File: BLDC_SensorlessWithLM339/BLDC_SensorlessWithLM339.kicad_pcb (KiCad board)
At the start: 2 copper layers, 48 parts, among them J1 Conn_01x04_Female, J2 Conn_01x07_Female, J3 Screw_Terminal_01x02, J4 Screw_Terminal_01x03, Q1 50N06, Q2 50N06, Q3 50N06, Q4 50N06, Q5 50N06, Q6 50N06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

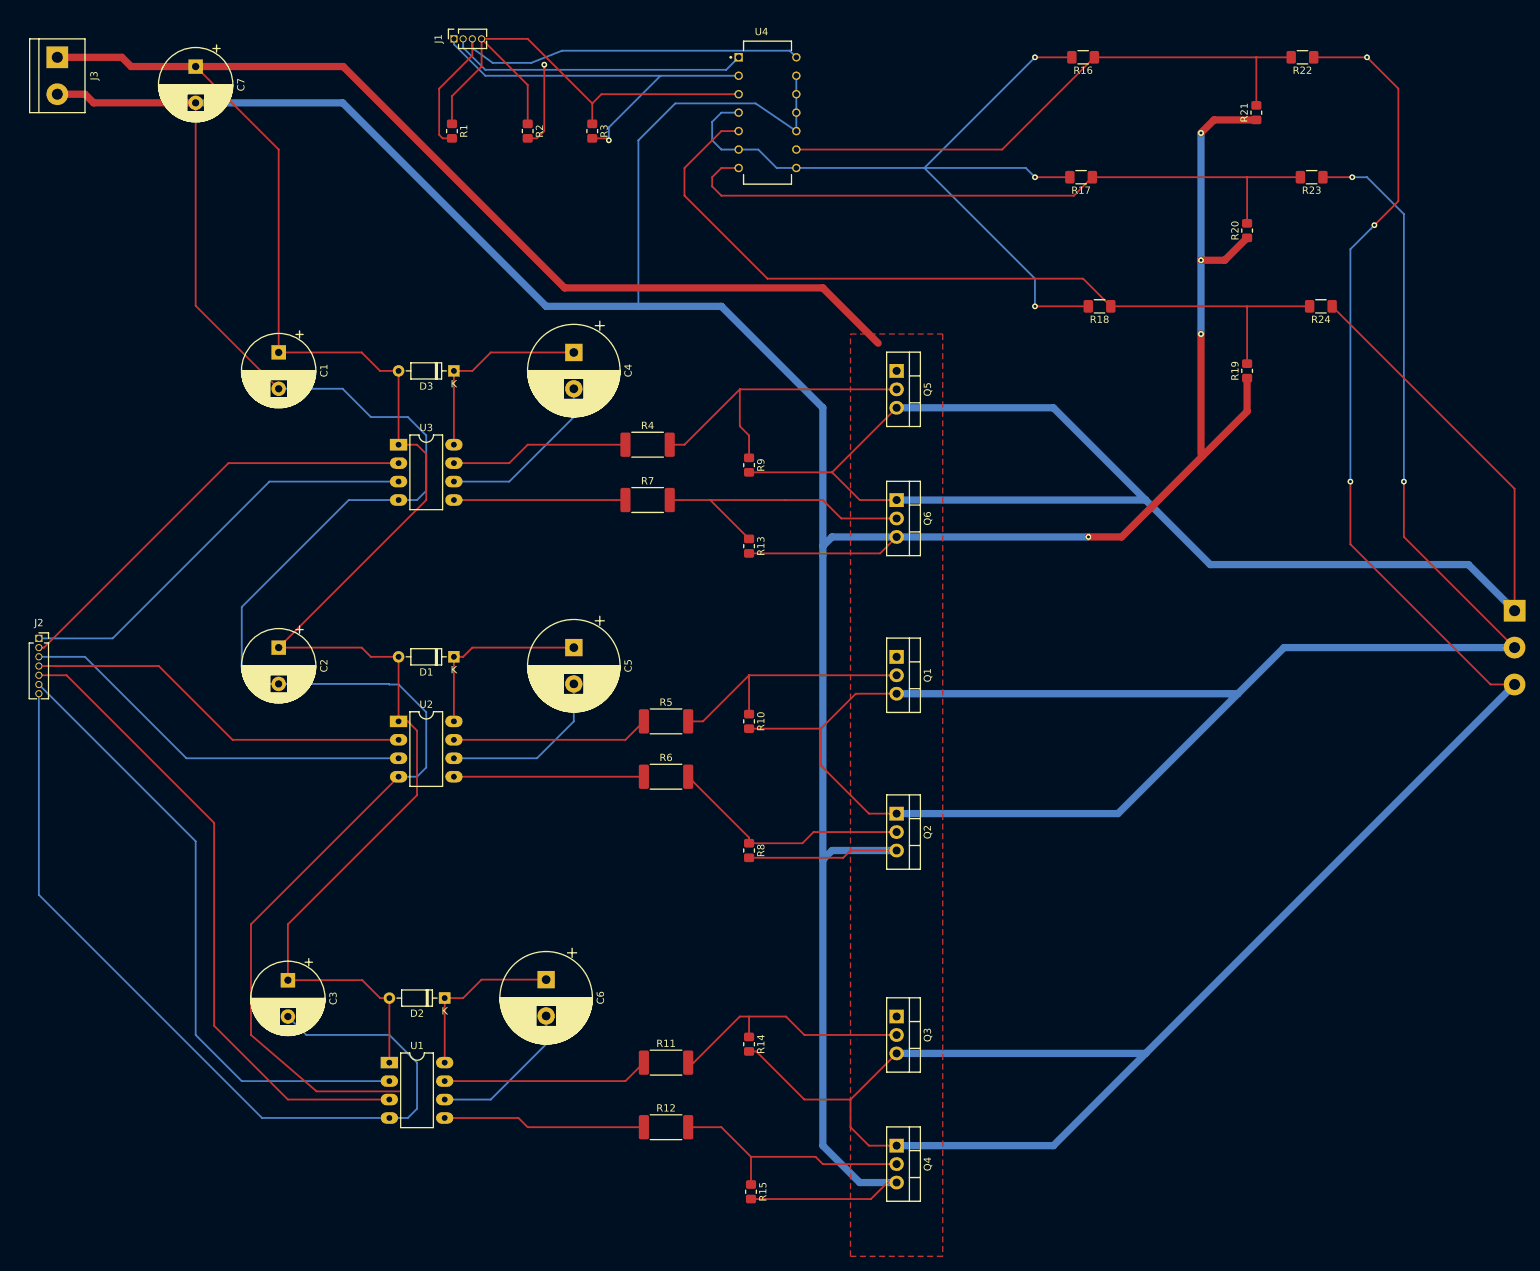
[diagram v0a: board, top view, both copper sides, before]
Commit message: Updated to Version 0.2
Updated to version 0.2. Now pcb holds only 10x10 cm^2 field.
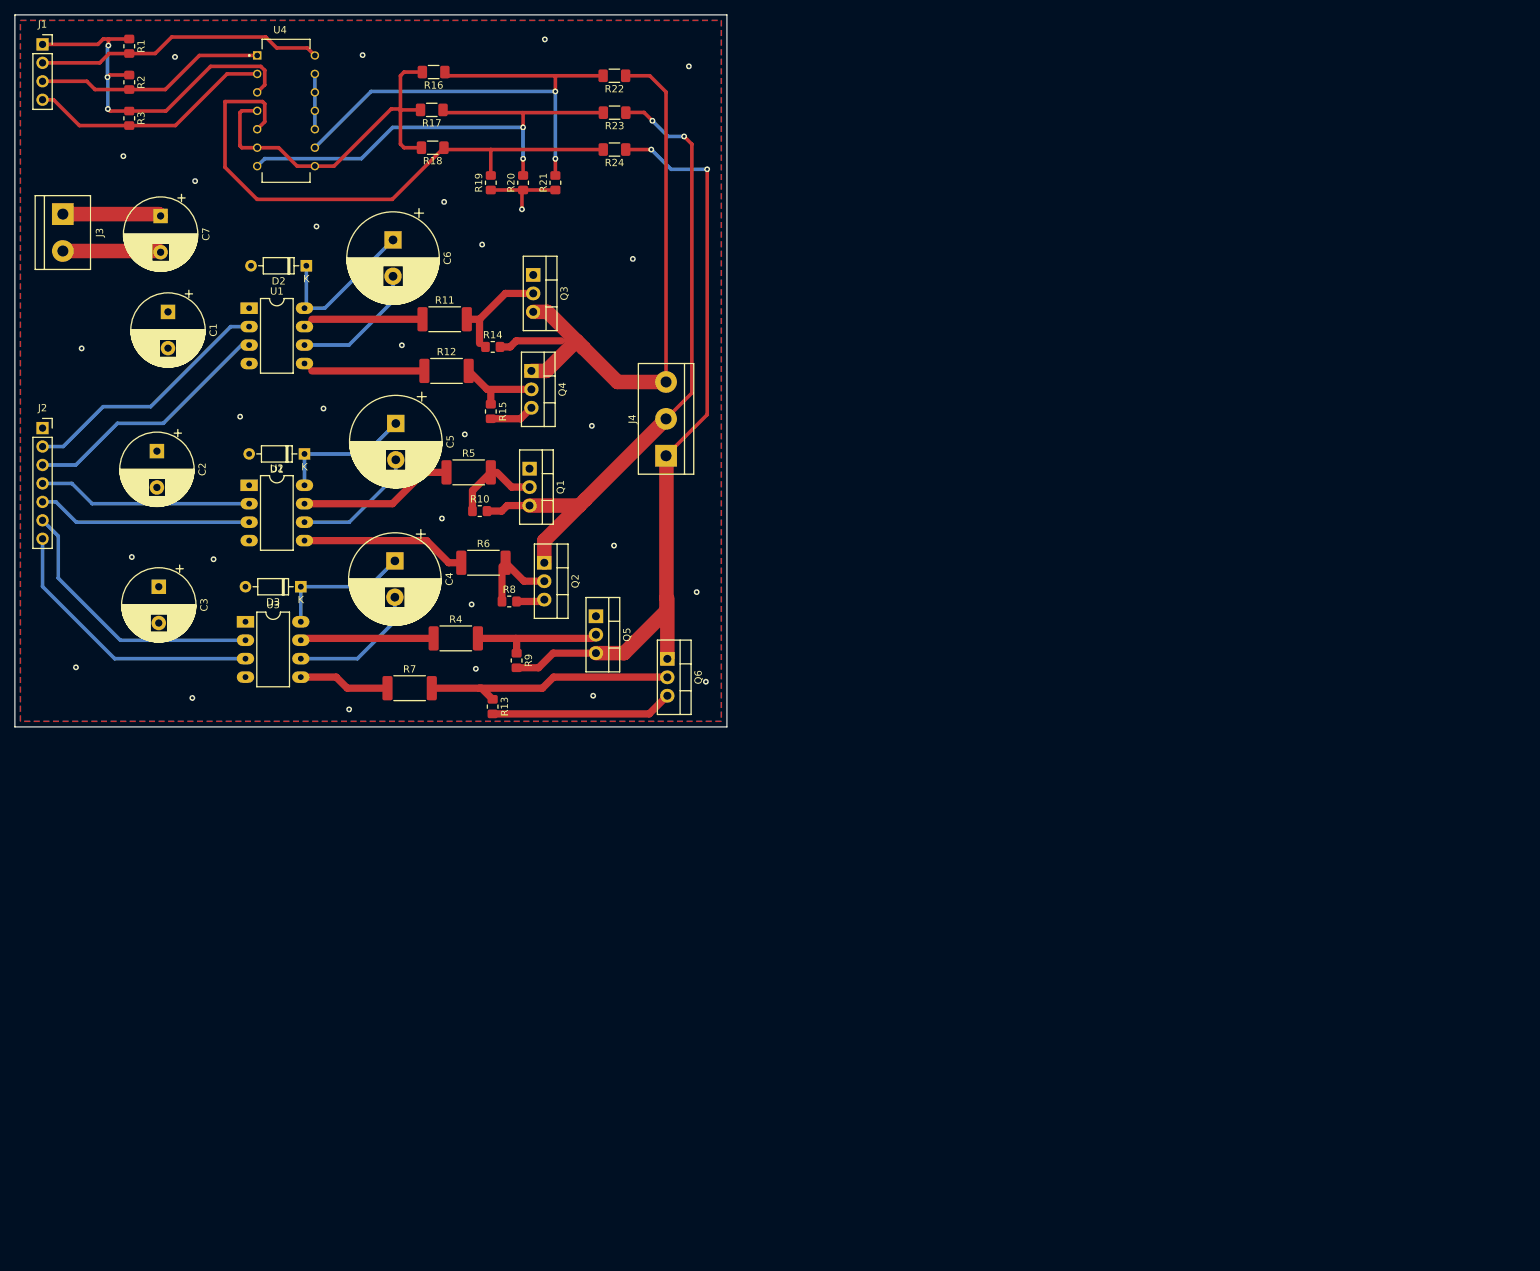
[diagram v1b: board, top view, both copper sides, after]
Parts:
- J1: footprint Connector_PinSocket_1.27mm:PinSocket_1x04_P1.27mm_Vertical -> Connector_PinSocket_2.54mm:PinSocket_1x04_P2.54mm_Vertical
- J2: footprint Connector_PinSocket_1.27mm:PinSocket_1x07_P1.27mm_Vertical -> Connector_PinSocket_2.54mm:PinSocket_1x07_P2.54mm_Vertical
- J4: moved to F.Cu
- moved J4 118.8 mm to (101.6, 72.6), turned to 90 degrees
- moved Q4 117.9 mm to (83.1, 61.0)
- moved Q3 113.7 mm to (83.3, 47.8)
- moved R15 113.3 mm to (77.5, 66.5)
- moved R12 108.4 mm to (71.4, 61.0)
- moved R19 107.3 mm to (77.5, 35.1)
- moved R11 106.8 mm to (71.1, 53.8)
- moved U1 105.7 mm to (44.2, 52.3)
- moved C6 104.0 mm to (64.0, 42.9)
- moved D2 102.6 mm to (52.1, 46.5)
- moved R14 102.3 mm to (77.7, 57.7), turned to 0 degrees
- moved R20 99.9 mm to (81.9, 35.1)
- moved R24 99.6 mm to (94.5, 30.5)
- moved R21 97.0 mm to (86.4, 35.1)
- moved R23 96.4 mm to (94.5, 25.4)
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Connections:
- J1 pad 1: Net-(J1-Pad1) -> +3V3
- J1 pad 4: +3V3 -> Net-(J1-Pad4)
- J2 pad 7: GND -> Net-(J2-Pad7)
- R1 pad 2: Net-(J1-Pad3) -> Net-(J1-Pad2)
- R2 pad 2: Net-(J1-Pad2) -> Net-(J1-Pad3)
- R3 pad 2: Net-(J1-Pad1) -> Net-(J1-Pad4)
- U1 pad 2: Net-(J2-Pad6) -> Net-(J2-Pad2)
- U1 pad 3: Net-(J2-Pad5) -> Net-(J2-Pad3)
- U2 pad 3: Net-(J2-Pad3) -> Net-(J2-Pad5)
- U3 pad 2: Net-(J2-Pad2) -> Net-(J2-Pad6)
- U3 pad 3: Net-(J2-Pad1) -> Net-(J2-Pad7)
- U4 pad 1: Net-(J1-Pad2) -> Net-(J1-Pad3)
- U4 pad 14: Net-(J1-Pad3) -> Net-(J1-Pad2)
- U4 pad 2: Net-(J1-Pad1) -> Net-(J1-Pad4)
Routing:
- net GND: track 841.6 -> 68.0 mm, vias 4 -> 29
- net +12V: track 335.2 -> 13.6 mm
- net Net-(J4-Pad3): track 292.1 -> 89.1 mm, vias 3 -> 0
- net Net-(J4-Pad2): track 261.4 -> 91.2 mm
- net Net-(J4-Pad1): track 217.7 -> 107.8 mm, vias 0 -> 2
- net Net-(R16-Pad2): track 117.4 -> 52.1 mm, vias 3 -> 0
- net Net-(J2-Pad5): track 88.8 -> 29.6 mm
- net Net-(J2-Pad1): track 58.5 -> 0.00 mm
- net Net-(J1-Pad1): track 56.0 -> 0.00 mm, vias 1 -> 0
- net Net-(J2-Pad6): track 86.5 -> 38.2 mm
- net Net-(J2-Pad7): track 0.00 -> 38.6 mm
- net Net-(R18-Pad1): track 113.7 -> 79.1 mm
- net Net-(J1-Pad4): track 0.00 -> 34.0 mm
- net Net-(J1-Pad3): track 64.3 -> 32.0 mm
- net Net-(Q5-Pad2): track 44.4 -> 18.6 mm
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- added copper zone on B.Cu, net GND
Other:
- board outline added: 98 x 98 mm
- net class Default: trace_width 0.25 -> 0.5
- net class PWR_12V added: clearance 0.5, trace_width 2, via_dia 1.6, via_drill 1
